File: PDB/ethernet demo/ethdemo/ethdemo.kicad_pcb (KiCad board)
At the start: 2 copper layers, 38 parts, among them Q1 CSD19538Q3AT, U1 STM32H742VGTx, U3 TPS23861PWR, Y1 25MHz

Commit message: Finished first draft of demo schem
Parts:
- added C12: 0.1uF, Capacitor_SMD:C_0603_1608Metric, F.Cu at (42.6, 70.5)
- added C15: 0.1uF, Capacitor_SMD:C_0603_1608Metric, F.Cu at (62.5, 53.0)
- added C16: 0.1uF, Capacitor_SMD:C_0603_1608Metric, F.Cu at (62.5, 55.5)
- added C17: 0.1uF, Capacitor_SMD:C_0603_1608Metric, F.Cu at (62.5, 58.1)
- added C18: 0.1uF, Capacitor_SMD:C_0603_1608Metric, F.Cu at (62.5, 60.6)
- added C19: 10uF, Capacitor_SMD:C_0603_1608Metric, F.Cu at (62.5, 63.1)
- added C20: 1nF, Capacitor_SMD:C_0603_1608Metric, F.Cu at (62.5, 65.6)
- added C21: 1nF, Capacitor_SMD:C_0603_1608Metric, F.Cu at (62.5, 68.1)
- added C22: 0.1uF, Capacitor_SMD:C_0603_1608Metric, F.Cu at (62.5, 70.6)
- added C23: 0.1uF, Capacitor_SMD:C_0603_1608Metric, F.Cu at (62.5, 73.1)
- added C24: 10pF, Capacitor_SMD:C_0603_1608Metric, F.Cu at (62.5, 75.6)
- added C25: 10pF, Capacitor_SMD:C_0603_1608Metric, F.Cu at (66.5, 50.5)
- added C26: 10uF, Capacitor_SMD:C_0603_1608Metric, F.Cu at (66.5, 53.0)
- added C27: 0.1uF, Capacitor_SMD:C_0603_1608Metric, F.Cu at (66.5, 55.5)
- added C28: 22uF, Capacitor_SMD:C_0603_1608Metric, F.Cu at (66.5, 58.1)
- added C29: 22uF, Capacitor_SMD:C_0603_1608Metric, F.Cu at (66.5, 60.6)
- added C30: 0.1uF, Capacitor_SMD:C_0603_1608Metric, F.Cu at (66.5, 63.1)
- added C31: 22uF, Capacitor_SMD:C_0603_1608Metric, F.Cu at (66.5, 65.6)
- added C32: 0.1uF, Capacitor_SMD:C_0603_1608Metric, F.Cu at (66.5, 68.1)
- added C33: 0.1uF, Capacitor_SMD:C_0603_1608Metric, F.Cu at (66.5, 70.6)
- added C34: 0.1uF, Capacitor_SMD:C_0603_1608Metric, F.Cu at (66.5, 73.1)
- added C35: 22uF, Capacitor_SMD:C_0603_1608Metric, F.Cu at (66.5, 75.6)
- added C36: 10uF, Capacitor_SMD:C_0603_1608Metric, F.Cu at (70.5, 50.5)
- added D6: SMCJ60A, foot:SMCJ60A, F.Cu at (38.1, 67.3)
- added D7: SMAJ4764A-TP, foot:SMAJ100CA_13_F, F.Cu at (32.5, 68.9)
- added J1: 0826-1X1T-GJ-F, foot:0826-1X1T-GJ-F, F.Cu at (70.8, 26.6)
- added J2: 0826-1X1T-GJ-F, foot:0826-1X1T-GJ-F, F.Cu at (91.4, 26.6)
- added R12: 49.9 Ohm, Resistor_SMD:R_0603_1608Metric, F.Cu at (70.5, 53.0)
- added R13: 49.9 Ohm, Resistor_SMD:R_0603_1608Metric, F.Cu at (70.5, 55.5)
- added R14: 49.9 Ohm, Resistor_SMD:R_0603_1608Metric, F.Cu at (70.5, 58.1)
- added R15: 49.9 Ohm, Resistor_SMD:R_0603_1608Metric, F.Cu at (70.5, 60.6)
- added R16: 11.8kOhm, Resistor_SMD:R_0603_1608Metric, F.Cu at (70.5, 63.1)
- added R17: 49.9 Ohm, Resistor_SMD:R_0603_1608Metric, F.Cu at (70.5, 65.6)
- added R18: 49.9 Ohm, Resistor_SMD:R_0603_1608Metric, F.Cu at (70.5, 68.1)
- added R19: 49.9 Ohm, Resistor_SMD:R_0603_1608Metric, F.Cu at (70.5, 70.6)
- added R20: 49.9 Ohm, Resistor_SMD:R_0603_1608Metric, F.Cu at (70.5, 73.1)
- added R21: 1kOhm, Resistor_SMD:R_0603_1608Metric, F.Cu at (70.5, 75.6)
- added R22: 1kOhm, Resistor_SMD:R_0603_1608Metric, F.Cu at (74.5, 50.5)
- added R23: 10kOhm, Resistor_SMD:R_0603_1608Metric, F.Cu at (74.5, 53.0)
- added R24: 22 Ohm, Resistor_SMD:R_0603_1608Metric, F.Cu at (74.5, 55.5)
- added R25: 22 Ohm, Resistor_SMD:R_0603_1608Metric, F.Cu at (74.5, 58.1)
- added R26: 22 Ohm, Resistor_SMD:R_0603_1608Metric, F.Cu at (74.5, 60.6)
- added R27: 22 Ohm, Resistor_SMD:R_0603_1608Metric, F.Cu at (74.5, 63.1)
- added R28: 22 Ohm, Resistor_SMD:R_0603_1608Metric, F.Cu at (74.5, 65.6)
- added R29: 22 Ohm, Resistor_SMD:R_0603_1608Metric, F.Cu at (74.5, 68.1)
- added R30: Interupt, Resistor_SMD:R_0603_1608Metric, F.Cu at (74.5, 70.6)
- added R31: 1kOhm, Resistor_SMD:R_0603_1608Metric, F.Cu at (74.5, 73.1)
- added R34: 1kOhm, Resistor_SMD:R_0603_1608Metric, F.Cu at (74.5, 75.6)
- added R35: 4.7kOhm, Resistor_SMD:R_0603_1608Metric, F.Cu at (78.5, 50.5)
- added R36: 4.7kOhm, Resistor_SMD:R_0603_1608Metric, F.Cu at (78.5, 53.0)
- added R37: 22 Ohm, Resistor_SMD:R_0603_1608Metric, F.Cu at (78.5, 55.5)
- added R38: 10kOhm, Resistor_SMD:R_0603_1608Metric, F.Cu at (78.5, 58.1)
- added R39: 10kOhm, Resistor_SMD:R_0603_1608Metric, F.Cu at (78.5, 60.6)
- added R40: 10kOhm, Resistor_SMD:R_0603_1608Metric, F.Cu at (78.5, 63.1)
- added R41: 10kOhm, Resistor_SMD:R_0603_1608Metric, F.Cu at (78.5, 65.6)
- added R42: 4.7kOhm, Resistor_SMD:R_0603_1608Metric, F.Cu at (78.5, 68.1)
- added R43: 220 Ohm, Resistor_SMD:R_0603_1608Metric, F.Cu at (78.5, 70.6)
- added R44: 220 Ohm, Resistor_SMD:R_0603_1608Metric, F.Cu at (78.5, 73.1)
- added R45: 220 Ohm, Resistor_SMD:R_0603_1608Metric, F.Cu at (78.5, 75.6)
- added R46: 220 Ohm, Resistor_SMD:R_0603_1608Metric, F.Cu at (82.5, 50.5)
- added R47: 1kOhm, Resistor_SMD:R_0603_1608Metric, F.Cu at (82.5, 53.0)
- added R48: 1kOhm, Resistor_SMD:R_0603_1608Metric, F.Cu at (82.5, 55.5)
- added R49: 1kOhm, Resistor_SMD:R_0603_1608Metric, F.Cu at (82.5, 58.1)
- added R50: 1kOhm, Resistor_SMD:R_0603_1608Metric, F.Cu at (82.5, 60.6)
- added U2: KSZ8863RLLI, foot:KSZ8863RLLI, F.Cu at (90.4, 63.6)
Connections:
- U1 pad 23: /UART4_RX -> /REF_CLK
- U1 pad 31: /MOSI -> /CRS_DV
- U1 pad 32: /PC4 -> /RXD0
- U1 pad 33: /PC5 -> /RXD1
- U1 pad 47: /PB11 -> /TX_EN
- U1 pad 51: Net-(U1-PB12) -> /TXD0
- U1 pad 52: Net-(U1-PB13) -> /TXD1
- U1 pad 92: unconnected-(U1-PB6-Pad92) -> /Clock
- U1 pad 93: unconnected-(U1-PB7-Pad93) -> /Data

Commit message: Started demo layout
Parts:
- removed R30: Interupt, Resistor_SMD:R_0603_1608Metric
- C23, C27, C30, C32, R16: moved to B.Cu
- moved J2 112.9 mm to (141.0, 128.0), turned to -90 degrees
- moved C21 107.5 mm to (143.4, 138.8), turned to 180 degrees
- moved J1 106.7 mm to (141.0, 106.9), turned to -90 degrees
- moved C26 102.1 mm to (123.4, 137.8)
- moved C36 84.4 mm to (107.2, 126.5), turned to 90 degrees
- moved C19 81.2 mm to (123.4, 116.7)
- moved C10 78.3 mm to (21.7, 136.4)
- moved R6 78.3 mm to (27.4, 153.1)
- moved C12 78.3 mm to (46.9, 148.7)
- moved D6 78.3 mm to (42.3, 145.5)
- moved R11 78.3 mm to (29.8, 148.4)
- moved R32 78.3 mm to (21.1, 139.9)
- moved R7 78.3 mm to (27.4, 151.5)
- moved R8 78.3 mm to (27.4, 150.0)
- moved C11 78.3 mm to (31.5, 136.7)
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
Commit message: worked on eth ic routing
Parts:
- removed D1, D2: LED, LED_SMD:LED_0805_2012Metric
- removed R1, R2: 270, Resistor_SMD:R_0603_1608Metric
- C15, C16, C22, C28, C29, C31, R12, R13, R14, R15, R21, R22, R31, R35, R36, R38, R39, R40, R41, R42, R43: moved to B.Cu
- D8: footprint Diode_THT:D_DO-41_SOD81_P10.16mm_Horizontal -> Diode_SMD:D_SMA
- moved D8 119.5 mm to (111.5, 127.7), turned to 90 degrees
- moved C15 87.6 mm to (116.3, 122.2), turned to 180 degrees
- moved C16 86.5 mm to (114.5, 124.6)
- moved R12 86.1 mm to (118.5, 124.5), turned to 90 degrees
- moved R13 83.2 mm to (117.0, 124.5), turned to 90 degrees
- moved R14 82.5 mm to (114.5, 127.8)
- moved R23 81.1 mm to (108.8, 126.5), turned to -90 degrees
- moved R15 79.0 mm to (114.5, 126.2)
- moved C28 77.6 mm to (106.0, 124.8), turned to 90 degrees
- moved C29 75.8 mm to (109.2, 123.1)
- moved R36 74.9 mm to (99.8, 124.8), turned to 90 degrees
- moved R35 74.8 mm to (95.6, 123.4), turned to 90 degrees
- moved R22 74.8 mm to (105.5, 118.6), turned to -90 degrees
- moved C17 72.6 mm to (112.9, 110.3)
- moved R43 68.8 mm to (122.7, 123.4), turned to 90 degrees
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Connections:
- net Net-(C24-Pad2) renamed /OSC1
- net Net-(J1-TRD1+) renamed /TX2+
- net Net-(J1-TRD1-) renamed /TX2-
- net Net-(J1-TRD2+) renamed /RX2+
- net Net-(J1-TRD2-) renamed /RX2-
- net Net-(J2-TRD1+) renamed /D1+
- net Net-(J2-TRD1-) renamed /D1-
- net Net-(J2-TRD2+) renamed /D2+
- net Net-(J2-TRD2-) renamed /D2-
- net Net-(U2-INTRN) renamed /Lost Connect
- C25 pad 1: Net-(C25-Pad1) -> /OSC0
- R47 pad 1: /P2LED0 -> +3.3V
- R47 pad 2: +3.3V -> /P2LED0
- U1 pad 12: unconnected-(U1-PH0-Pad12) -> /OSC0
- U1 pad 13: unconnected-(U1-PH1-Pad13) -> /OCS1
- Y1 pad 2: Net-(C25-Pad1) -> /OSC0
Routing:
- net /RX2-: track 0.00 -> 25.9 mm, vias 0 -> 1
- net /RX2+: track 0.00 -> 25.0 mm, vias 0 -> 1
- net /D1+: track 0.00 -> 21.7 mm, vias 0 -> 1
- net /D2-: track 0.00 -> 21.6 mm, vias 0 -> 1
- net /D2+: track 0.00 -> 21.4 mm, vias 0 -> 1
- net GND: track 0.00 -> 21.2 mm, vias 0 -> 8
- net /TX2+: track 0.00 -> 20.0 mm, vias 0 -> 1
- net /D1-: track 0.00 -> 19.0 mm, vias 0 -> 2
- net /TX2-: track 0.00 -> 18.3 mm
- net +3.3V: track 0.00 -> 15.7 mm, vias 0 -> 7
- net +1.8V: track 0.00 -> 9.74 mm, vias 0 -> 1
- net Net-(D8-A): track 0.00 -> 6.84 mm
- net Net-(U2-SMRXDV3): track 0.00 -> 5.03 mm, vias 0 -> 1
- net Net-(U2-SMRXD32): track 0.00 -> 4.88 mm, vias 0 -> 1
- net /Lost Connect: track 0.00 -> 4.71 mm, vias 0 -> 1
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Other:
- copper layers 2 -> 4

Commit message: mostly finished routing and board design
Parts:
- moved TP2 196.2 mm to (245.1, 40.1), turned to 90 degrees
- moved C10 195.2 mm to (210.1, 85.3)
- moved C11 195.2 mm to (219.9, 85.6)
- moved C12 195.2 mm to (235.2, 97.5)
- moved D7 195.2 mm to (225.2, 96.0)
- moved Q1 195.2 mm to (220.4, 101.0)
- moved R10 195.2 mm to (219.8, 97.2)
- moved R11 195.2 mm to (218.2, 97.3)
- moved R32 195.2 mm to (209.6, 88.8)
- moved R6 195.2 mm to (215.8, 101.9)
- moved R7 195.2 mm to (215.8, 100.4)
- moved R8 195.2 mm to (215.8, 98.9)
- moved R9 195.2 mm to (215.8, 97.4)
- moved U3 195.2 mm to (215.1, 90.6)
- moved D6 195.2 mm to (230.7, 94.4)
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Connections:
- net /RXD0 renamed /RX-
- net /RXD1 renamed /RX+
- net /TXD0 renamed /TX-
- net /TXD1 renamed /TX+
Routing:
- net GND: track 21.2 -> 105.7 mm, vias 8 -> 55
- net +3.3V: track 15.7 -> 88.4 mm, vias 7 -> 27
- net 48V: track 0.00 -> 56.7 mm
- net /Data: track 1.65 -> 55.2 mm, vias 1 -> 2
- net /Clock: track 2.33 -> 55.6 mm, vias 1 -> 4
- net V-: track 0.00 -> 45.0 mm
- net /P1LED1: track 0.00 -> 32.7 mm, vias 0 -> 1
- net /P2LED1: track 0.00 -> 32.2 mm, vias 0 -> 2
- net /REF_CLK: track 0.00 -> 27.7 mm, vias 0 -> 2
- net /TX-: track 0.00 -> 25.0 mm, vias 0 -> 3
- net /P2LED0: track 0.00 -> 23.5 mm, vias 0 -> 2
- net /TX+: track 0.00 -> 23.4 mm, vias 0 -> 2
- net /P1LED0: track 0.00 -> 21.4 mm
- net /TX_EN: track 0.00 -> 20.3 mm, vias 0 -> 2
- net /CRS_DV: track 0.00 -> 19.7 mm, vias 0 -> 2
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- added copper zone on In2.Cu, net +3.3V
- added copper zone on In1.Cu, net GND
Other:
- board outline added: 77.5 x 67.5 mm

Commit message: finished rev1
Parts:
- R31: moved to F.Cu
- moved R34 1.43 mm to (210.7, 77.7), turned to 180 degrees
- moved R31 0.20 mm to (205.8, 73.7)
- moved R47 0.06 mm to (226.1, 61.6)
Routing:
- net Net-(C16-Pad1): track 0.00 -> 3.24 mm
- net /D2+: track 21.1 -> 23.6 mm
- net /D2-: track 21.2 -> 22.3 mm
- net +3.3V: track 88.4 -> 89.0 mm
- net GND: track 105.7 -> 105.9 mm, vias 55 -> 54
- net /Clock: track 55.6 -> 55.7 mm, vias 4 -> 3

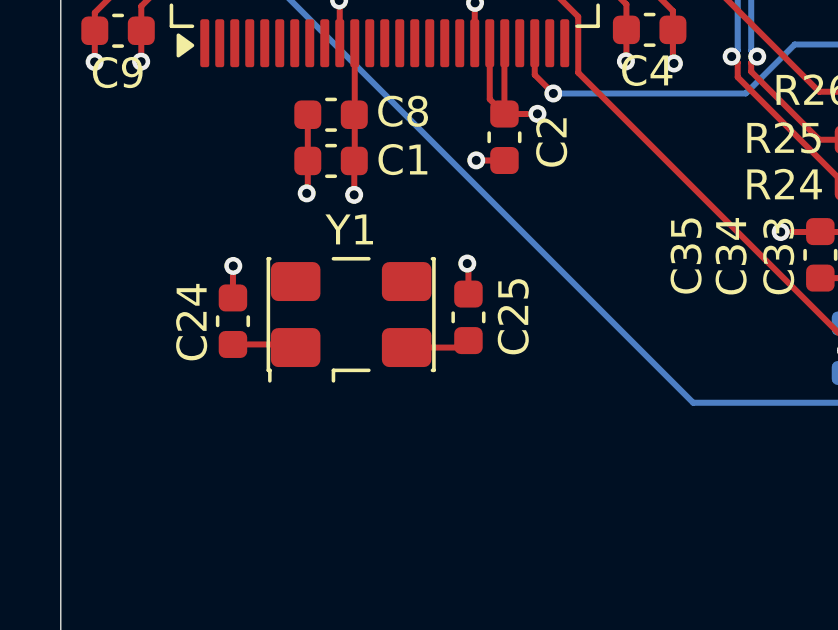
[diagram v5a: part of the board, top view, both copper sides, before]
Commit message: Fixed crystal footprint
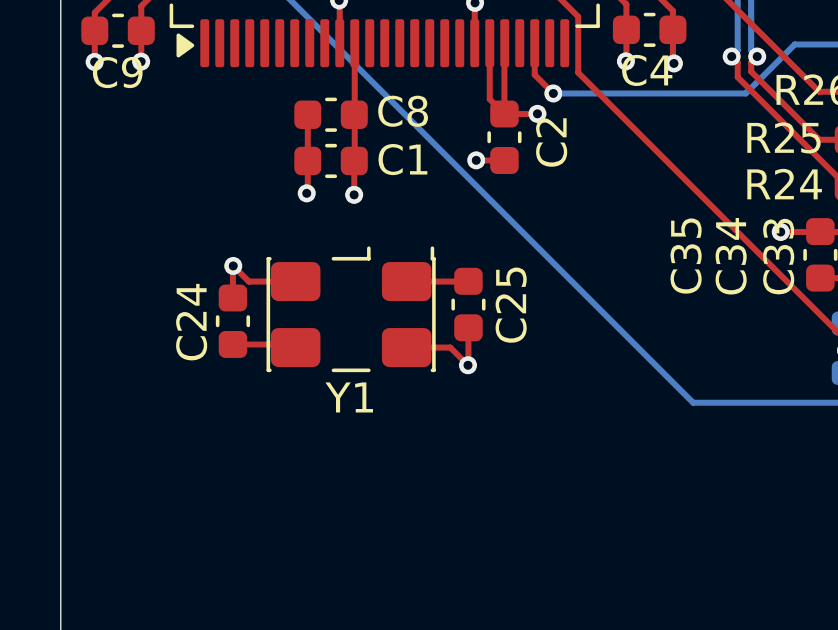
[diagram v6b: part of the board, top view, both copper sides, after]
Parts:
- moved C25 0.42 mm to (191.1, 72.0), turned to -90 degrees
- turned Y1 to 180 degrees
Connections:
- Y1 pad 1: /OSC1 -> /OSC0
- Y1 pad 2: /OSC0 -> GND
- Y1 pad 3: (no net) -> /OSC1
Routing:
- net GND: track 105.9 -> 110.7 mm

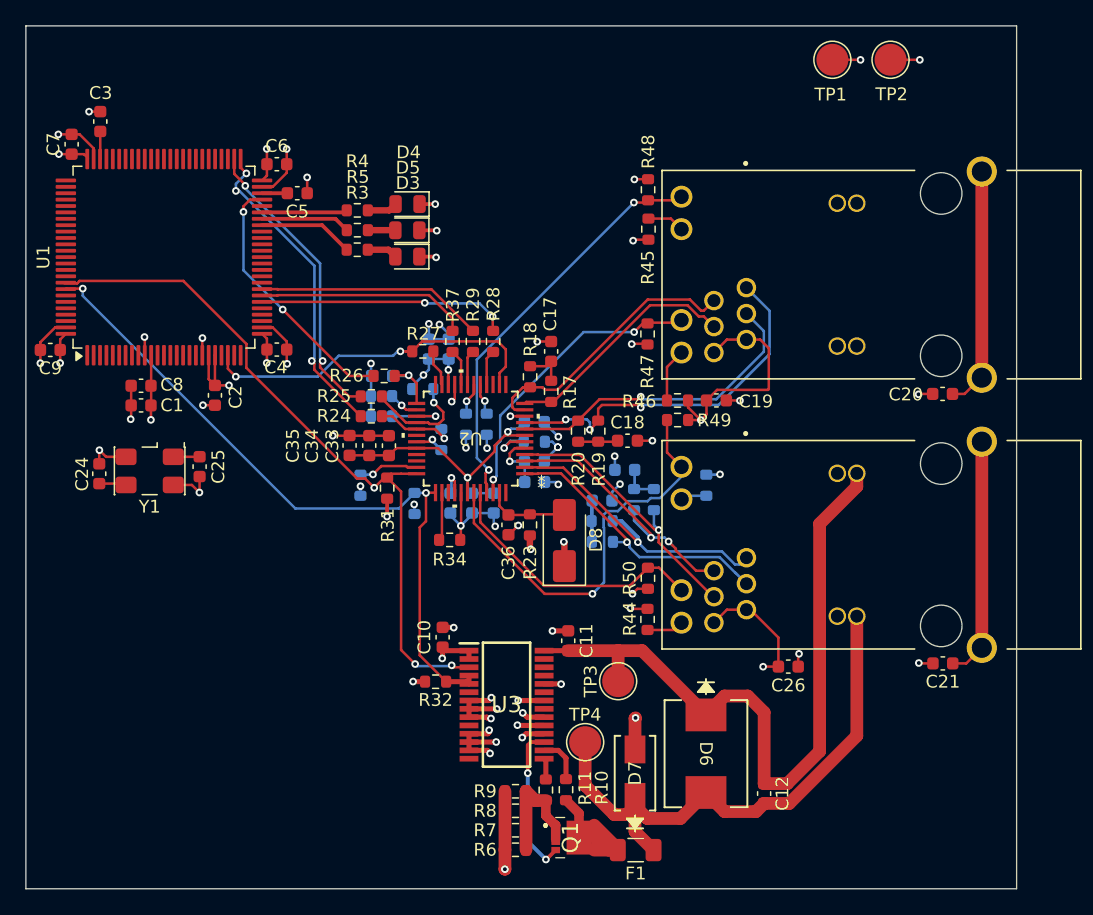
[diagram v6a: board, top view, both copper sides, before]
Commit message: did impedance and length tuning and control
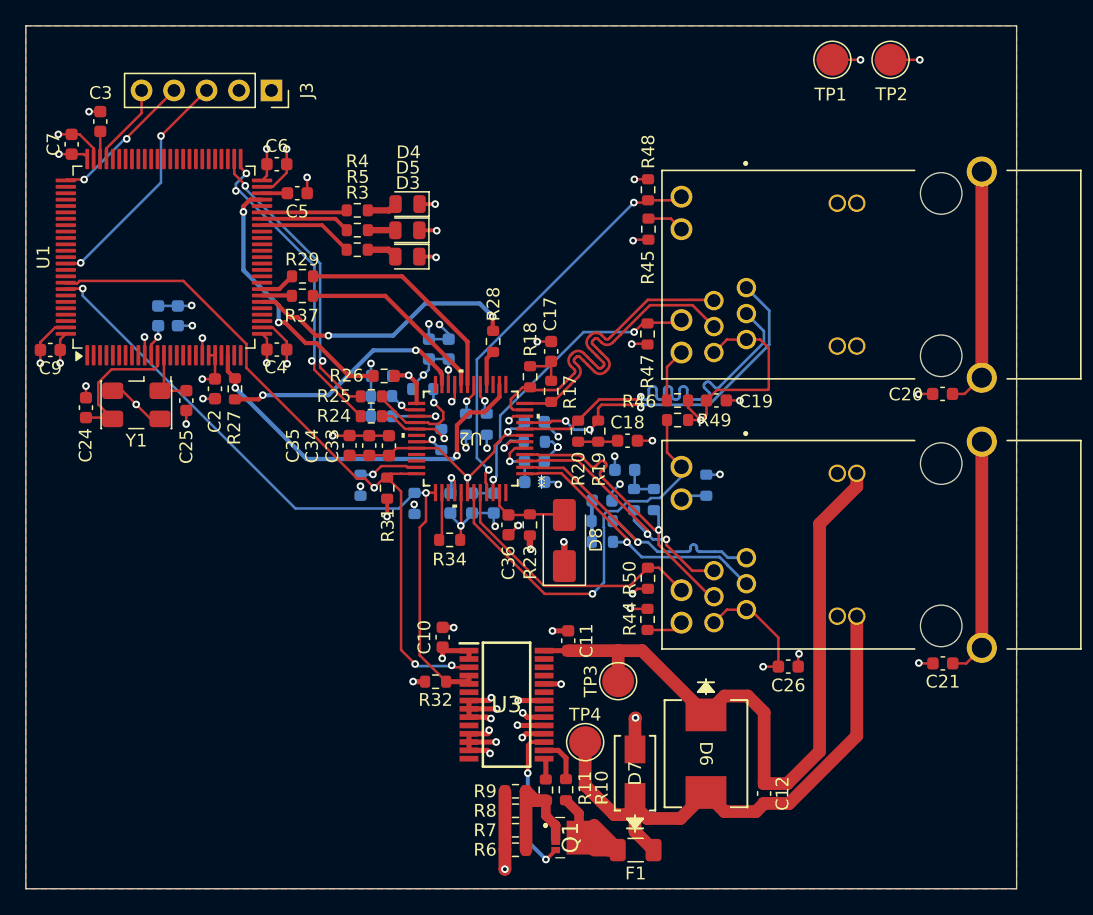
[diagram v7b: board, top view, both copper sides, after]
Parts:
- added J3: Conn_01x05_Socket, Connector_PinSocket_2.54mm:PinSocket_1x05_P2.54mm_Vertical, F.Cu at (196.7, 42.5)
- C1, C8: moved to B.Cu
- moved R27 15.0 mm to (193.8, 65.9), turned to 90 degrees
- moved R29 14.3 mm to (199.1, 57.1), turned to 180 degrees
- moved R37 12.3 mm to (199.1, 58.6), turned to 180 degrees
- moved C1 7.58 mm to (189.4, 60.2), turned to 90 degrees
- moved C8 5.63 mm to (187.8, 60.2), turned to 90 degrees
- moved C24 5.27 mm to (182.2, 67.4)
- moved Y1 5.27 mm to (186.1, 67.1)
- moved C25 5.27 mm to (190.1, 66.8)
- moved C2 0.51 mm to (192.3, 65.9)
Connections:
- C24 pad 2: /OSC1 -> /OSC0
- C25 pad 1: /OSC0 -> /OCS1
- Y1 pad 1: /OSC0 -> /OCS1
- Y1 pad 3: /OSC1 -> /OSC0
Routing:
- net /SWO/TRACE: track 0.00 -> 18.7 mm, vias 0 -> 2
- net Net-(U2-SMTXC3/REFCLKI_3): track 2.87 -> 19.4 mm, vias 0 -> 2
- net /RX+: track 17.9 -> 2.75 mm
- net Net-(U2-SMTXD31): track 2.72 -> 17.5 mm
- net /RX-: track 16.6 -> 2.34 mm
- net Net-(U2-SMTXD30): track 2.82 -> 15.0 mm
- net /SWCLK: track 0.00 -> 11.4 mm, vias 0 -> 2
- net /OSC0: track 2.06 -> 11.4 mm
- net /SWDIO: track 0.00 -> 6.50 mm
- net /TX2+: track 18.7 -> 24.6 mm
- net /RX2-: track 25.3 -> 31.0 mm
- net /TX2-: track 21.6 -> 26.9 mm
- net /OCS1: track 0.00 -> 5.24 mm
- net +3.3V: track 89.0 -> 85.1 mm, vias 27 -> 28
- net /REF_CLK: track 27.4 -> 30.1 mm
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- added copper zone on F.Cu, net GND
